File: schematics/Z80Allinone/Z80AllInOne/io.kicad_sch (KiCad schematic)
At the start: 30 parts, among them J1 USB_B_Micro, J2 IDC_IO_CONN, Q1 IRLML6402, SW1 SW_DIP_x04, U13 7400, U4 82C55A, U5 16550, U6 FT232RL

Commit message: Latest changes for adapt source to support Z80AllInOne adding some macros and latest schematic improvements
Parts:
- J2: value IDC_IO_CONN -> USER_IO_CONN
- JP1: value USB_POWER -> USB_POWER_SW
- R4, R5, R6, R7: value R -> 1K2
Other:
- sheet Casette Interface ports: added PPI_INT; removed none
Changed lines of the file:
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@@
+    (stroke (width 0) (type default) (color 0 0 0 0))
+  )
+  (wire (pts (xy 85.09 186.69) (xy 87.63 186.69))
     (stroke (width 0) (type default) (color 0 0 0 0))
   )
@@
   )
   (wire (pts (xy 259.08 55.88) (xy 259.08 80.01))
+    (stroke (width 0) (type default) (color 0 0 0 0))
+  )
+  (wire (pts (xy 85.09 175.26) (xy 85.09 186.69))
     (stroke (width 0) (type default) (color 0 0 0 0))
   )
@@
     (effects (font (size 1.27 1.27)) (justify left bottom))
   )
-  (label "PA4" (at 77.47 68.58 0)
+  (label "PA4" (at 80.01 68.58 0)
     (effects (font (size 1.27 1.27)) (justify left bottom))
   )
@@
     (effects (font (size 1.27 1.27)) (justify left bottom))
   )
-  (label "PA5" (at 77.47 71.12 0)
+  (label "PA5" (at 80.01 71.12 0)
     (effects (font (size 1.27 1.27)) (justify left bottom))
   )
@@
   (hierarchical_label "RESET_IO" (shape input) (at 123.19 140.97 270)
     (effects (font (size 1.27 1.27)) (justify right))
+  )
+  (hierarchical_label "PPI_INT" (shape output) (at 87.63 186.69 0)
+    (effects (font (size 1.27 1.27)) (justify left))
   )
   (hierarchical_label "RESET_IO" (shape input) (at 29.21 58.42 180)
@@
   (symbol (lib_id "Device:R") (at 74.93 45.72 180) (unit 1)
     (in_bom yes) (on_board yes)
-    (property "Reference" "R4" (id 0) (at 76.708 44.5516 0)
-      (effects (font (size 1.27 1.27)) (justify right))
-    )
-    (property "Value" "R" (id 1) (at 76.708 46.863 0)
+    (property "Reference" "R4" (id 0) (at 73.66 41.91 0)
+      (effects (font (size 1.27 1.27)) (justify right))
+    )
+    (property "Value" "1K2" (id 1) (at 74.93 46.99 90)
       (effects (font (size 1.27 1.27)) (justify right))
     )
@@
       (effects (font (size 1.27 1.27)) (justify right))
     )
-    (property "Value" "USB_POWER" (id 1) (at 196.85 132.0799 90)
+    (property "Value" "USB_POWER_SW" (id 1) (at 196.85 132.0799 90)
       (effects (font (size 1.27 1.27)) (justify right))
     )
@@
     (in_bom yes) (on_board yes) (fields_autoplaced)
     (property "Reference" "J2" (id 0) (at 36.83 152.4 0))
-    (property "Value" "IDC_IO_CONN" (id 1) (at 36.83 154.94 0))
+    (property "Value" "USER_IO_CONN" (id 1) (at 36.83 154.94 0))
     (property "Footprint" "Connector_PCBEdge:EdgeConector_18pin" (id 2) (at 35.56 163.83 0)
       (effects (font (size 1.27 1.27)) hide)
@@
   (symbol (lib_id "Device:R") (at 82.55 45.72 180) (unit 1)
     (in_bom yes) (on_board yes)
-    (property "Reference" "R6" (id 0) (at 84.328 44.5516 0)
-      (effects (font (size 1.27 1.27)) (justify right))
-    )
-    (property "Value" "R" (id 1) (at 84.328 46.863 0)
+    (property "Reference" "R6" (id 0) (at 81.28 41.91 0)
+      (effects (font (size 1.27 1.27)) (justify right))
+    )
+    (property "Value" "1K2" (id 1) (at 82.55 46.99 90)
       (effects (font (size 1.27 1.27)) (justify right))
     )
@@
   (symbol (lib_id "Device:R") (at 78.74 45.72 180) (unit 1)
     (in_bom yes) (on_board yes)
-    (property "Reference" "R5" (id 0) (at 80.518 44.5516 0)
-      (effects (font (size 1.27 1.27)) (justify right))
-    )
-    (property "Value" "R" (id 1) (at 80.518 46.863 0)
+    (property "Reference" "R5" (id 0) (at 77.47 41.91 0)
+      (effects (font (size 1.27 1.27)) (justify right))
+    )
+    (property "Value" "1K2" (id 1) (at 78.74 46.99 90)
       (effects (font (size 1.27 1.27)) (justify right))
     )
@@
   (symbol (lib_id "Device:R") (at 86.36 45.72 180) (unit 1)
     (in_bom yes) (on_board yes)
-    (property "Reference" "R7" (id 0) (at 88.138 44.5516 0)
-      (effects (font (size 1.27 1.27)) (justify right))
-    )
-    (property "Value" "R" (id 1) (at 88.138 46.863 0)
+    (property "Reference" "R7" (id 0) (at 85.09 41.91 0)
+      (effects (font (size 1.27 1.27)) (justify right))
+    )
+    (property "Value" "1K2" (id 1) (at 86.36 46.99 90)
       (effects (font (size 1.27 1.27)) (justify right))
     )
@@
       (effects (font (size 1.27 1.27)) (justify right))
     )
-  )
+    (pin "PPI_INT" output (at 85.09 175.26 270)
+      (effects (font (size 1.27 1.27)) (justify left))
+    )
+  )

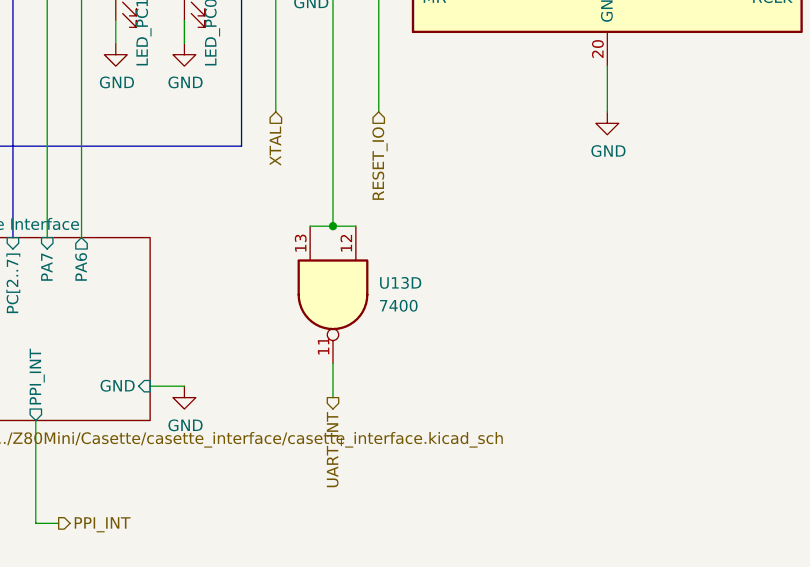
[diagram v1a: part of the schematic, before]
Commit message: Latest changes and replace CTC for 8253 PIT
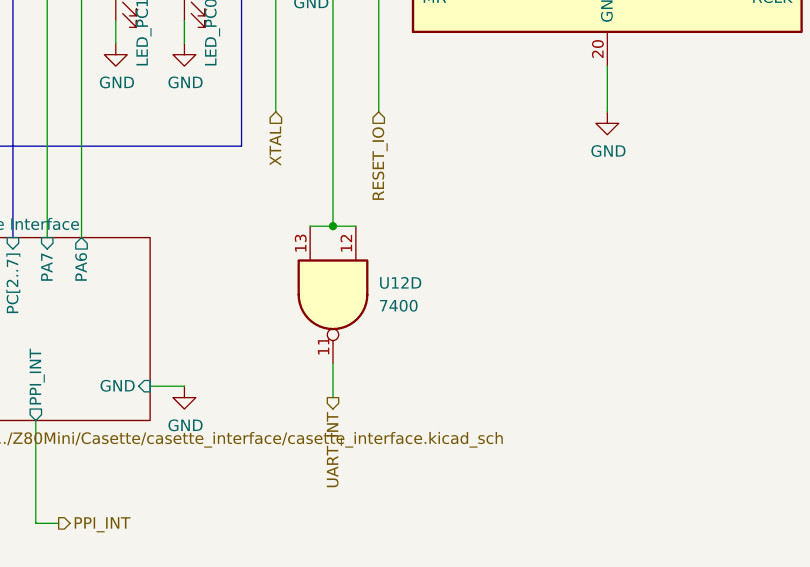
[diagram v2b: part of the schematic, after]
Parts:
- renumbered U13 to U12
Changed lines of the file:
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@@
   (symbol (lib_id "74xx:7400") (at 118.11 161.29 270) (unit 4)
     (in_bom yes) (on_board yes) (fields_autoplaced)
-    (property "Reference" "U13" (id 0) (at 123.19 160.0199 90)
+    (property "Reference" "U12" (id 0) (at 123.19 160.0199 90)
       (effects (font (size 1.27 1.27)) (justify left))
     )
